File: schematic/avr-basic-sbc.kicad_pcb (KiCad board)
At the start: 2 copper layers, 94 x 55 mm, 38 parts, among them J1 DC-005 Power Jack, J2 PS/2 keyboard port, J3 RCA Video Jack, J4 Port B, J5 Port A, J6 Port C, J7 Port D, J8 USBasp header, J9 Power output header, U1 ATmega1284P-P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

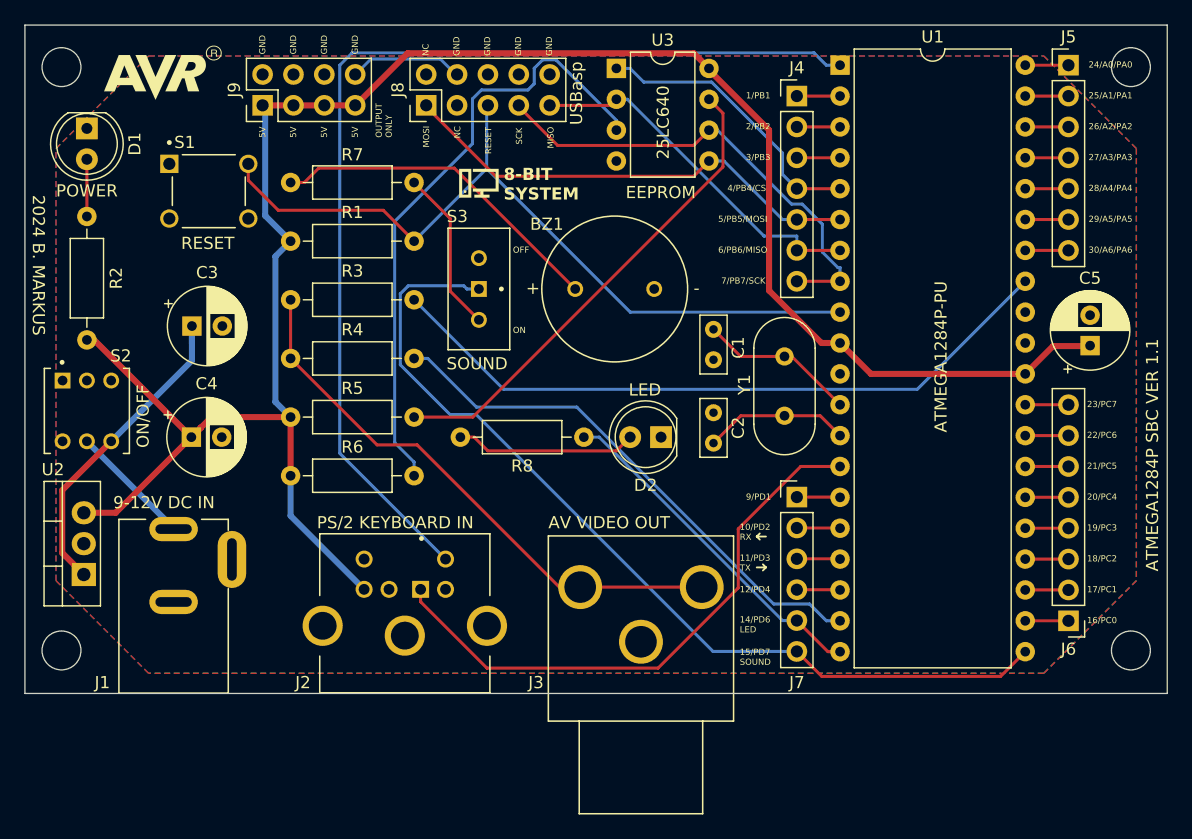
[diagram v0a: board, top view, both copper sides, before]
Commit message: AVR-SBC board updated - GPIO headers and IC-s realigned to match 0.254mm grid
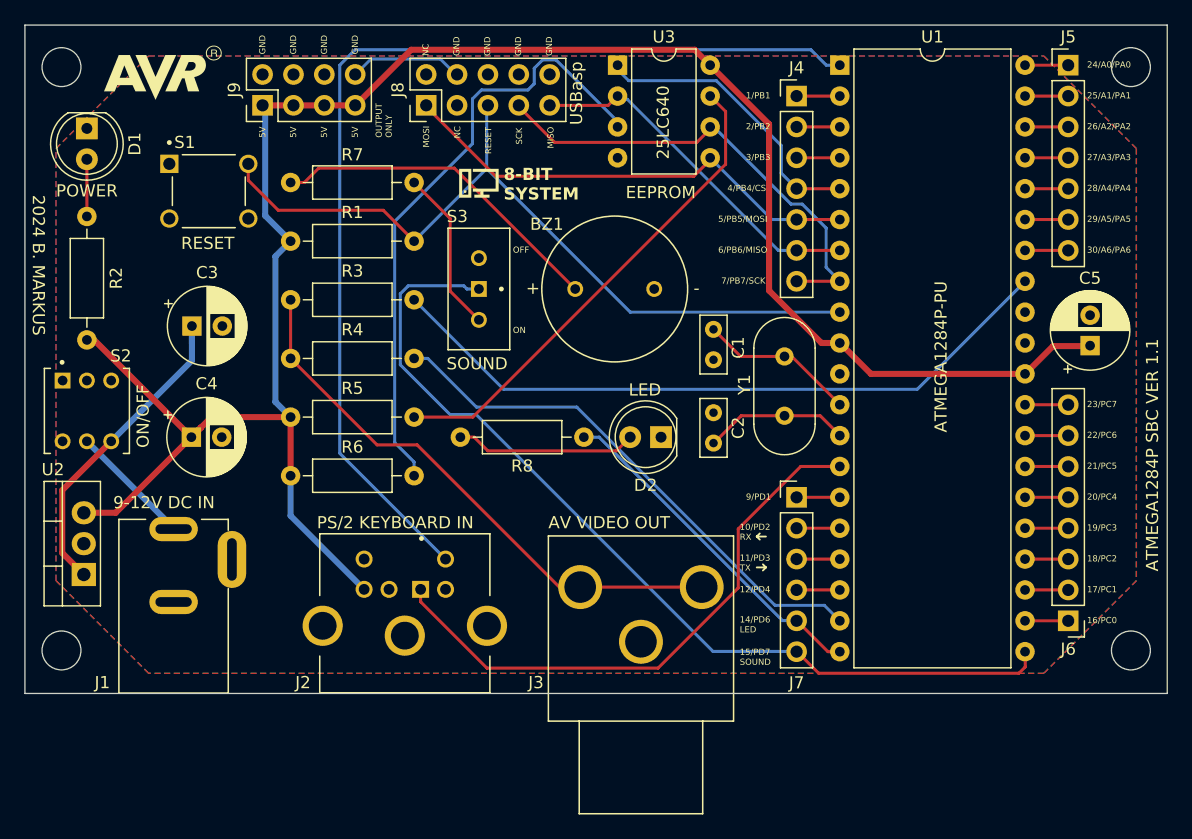
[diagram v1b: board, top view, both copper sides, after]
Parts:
- moved U3 0.28 mm to (48.8, 3.30)
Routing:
- net Net-(J7-Pin_6): track 75.6 -> 76.1 mm

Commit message: AVR-SBC board updated - Silkscreen updates and fill zones updated to match 1mm grid
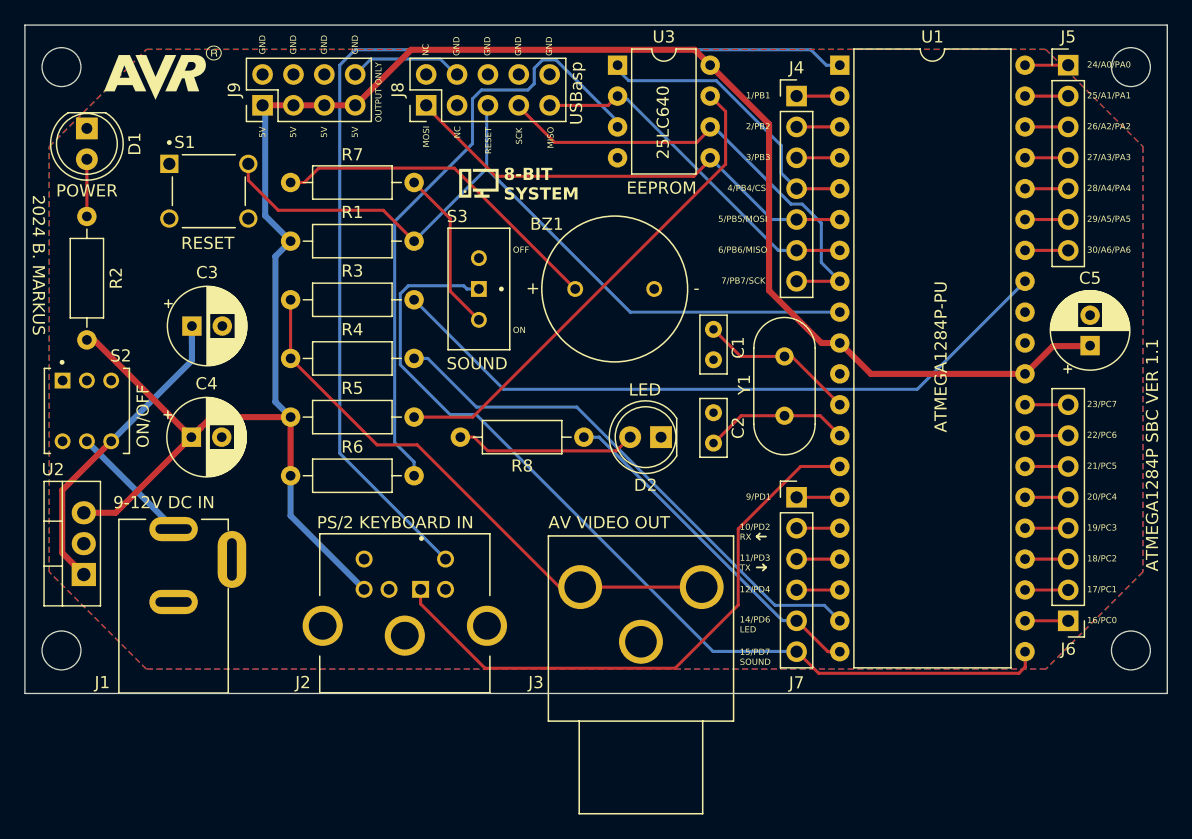
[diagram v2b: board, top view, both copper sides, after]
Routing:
- net Data: track 47.5 -> 48.4 mm
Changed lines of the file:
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@@
     (effects (font (size 0.508 0.508) (thickness 0.127)) (justify left bottom))
   )
-  (gr_text "OUTPUT\nONLY" (at 30.246 9.271 90) (layer "F.SilkS")
+  (gr_text "OUTPUT ONLY" (at 29.4 8 90) (layer "F.SilkS")
     (effects (font (size 0.508 0.508) (thickness 0.127)) (justify left bottom))
   )
@@
     (effects (font (size 0.508 0.508) (thickness 0.127)) (justify left bottom))
   )
-  (gr_text "EEPROM" (at 49.433 14.361) (layer "F.SilkS")
+  (gr_text "EEPROM" (at 49.5 14) (layer "F.SilkS")
     (effects (font (size 1 1) (thickness 0.15)) (justify left bottom))
   )
@@
   (segment (start 13.744 26.1854) (end 13.7442 26.1852) (width 0.5) (layer "B.Cu") (net 8))
   (segment (start 7.1 34.25) (end 13.744 27.6058) (width 0.5) (layer "B.Cu") (net 8))
-  (segment (start 58.6965 46.3158) (end 52.0945 52.9178) (width 0.25) (layer "F.Cu") (net 9))
-  (segment (start 38.0219 52.9178) (end 32.562 47.4579) (width 0.25) (layer "F.Cu") (net 9))
+  (segment (start 67.076 36.322) (end 63.8363 36.322) (width 0.25) (layer "F.Cu") (net 9))
+  (segment (start 58.6965 47.7295) (end 53.5082 52.9178) (width 0.25) (layer "F.Cu") (net 9))
+  (segment (start 53.5082 52.9178) (end 37.84985 52.9178) (width 0.25) (layer "F.Cu") (net 9))
+  (segment (start 37.84985 52.9178) (end 32.562 47.62995) (width 0.25) (layer "F.Cu") (net 9))
   (segment (start 63.8363 36.322) (end 58.6965 41.4618) (width 0.25) (layer "F.Cu") (net 9))
-  (segment (start 32.562 46.432) (end 32.562 47.4579) (width 0.25) (layer "F.Cu") (net 9))
-  (segment (start 52.0945 52.9178) (end 38.0219 52.9178) (width 0.25) (layer "F.Cu") (net 9))
-  (segment (start 67.076 36.322) (end 63.8363 36.322) (width 0.25) (layer "F.Cu") (net 9))
-  (segment (start 58.6965 41.4618) (end 58.6965 46.3158) (width 0.25) (layer "F.Cu") (net 9))
+  (segment (start 58.6965 41.4618) (end 58.6965 47.7295) (width 0.25) (layer "F.Cu") (net 9))
+  (segment (start 32.562 47.62995) (end 32.562 46.432) (width 0.25) (layer "F.Cu") (net 9))
   (segment (start 67.076 3.302) (end 65.9491 3.302) (width 0.25) (layer "B.Cu") (net 10))
   (segment (start 25.908 3.302) (end 25.908 35.238) (width 0.25) (layer "B.Cu") (net 10))
@@
   (segment (start 63.52 21.082) (end 67.076 21.082) (width 0.25) (layer "F.Cu") (net 17))
   (segment (start 63.03665 14.732) (end 63.9656 14.732) (width 0.25) (layer "B.Cu") (net 17))
+  (segment (start 63.9656 14.732) (end 65.532 16.2984) (width 0.25) (layer "B.Cu") (net 17))
+  (segment (start 56.95065 8.646) (end 63.03665 14.732) (width 0.25) (layer "B.Cu") (net 17))
+  (segment (start 65.532 19.538) (end 67.076 21.082) (width 0.25) (layer "B.Cu") (net 17))
   (segment (start 56.291 8.646) (end 56.95065 8.646) (width 0.25) (layer "B.Cu") (net 17))
-  (segment (start 63.9656 14.732) (end 65.931 16.6974) (width 0.25) (layer "B.Cu") (net 17))
-  (segment (start 65.931 19.937) (end 67.076 21.082) (width 0.25) (layer "B.Cu") (net 17))
-  (segment (start 56.95065 8.646) (end 63.03665 14.732) (width 0.25) (layer "B.Cu") (net 17))
-  (segment (start 65.931 16.6974) (end 65.931 19.937) (width 0.25) (layer "B.Cu") (net 17))
+  (segment (start 65.532 16.2984) (end 65.532 19.538) (width 0.25) (layer "B.Cu") (net 17))
   (segment (start 82.316 3.302) (end 85.872 3.302) (width 0.25) (layer "F.Cu") (net 18))
   (segment (start 82.316 5.842) (end 85.872 5.842) (width 0.25) (layer "F.Cu") (net 19))
@@
     (polygon
       (pts
-        (xy 2.56 10.16)
-        (xy 10.18 2.54)
-        (xy 83.84 2.54)
-        (xy 91.46 10.16)
-        (xy 91.46 45.72)
-        (xy 83.84 53.34)
-        (xy 10.18 53.34)
-        (xy 2.56 45.72)
+        (xy 2 10)
+        (xy 10 2)
+        (xy 84 2)
+        (xy 92 10)
+        (xy 92 45)
+        (xy 84 53)
+        (xy 10 53)
+        (xy 2 45)
       )
     )

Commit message: AVR-SBC board updated - Mounting holes aligned to match 1mm grid
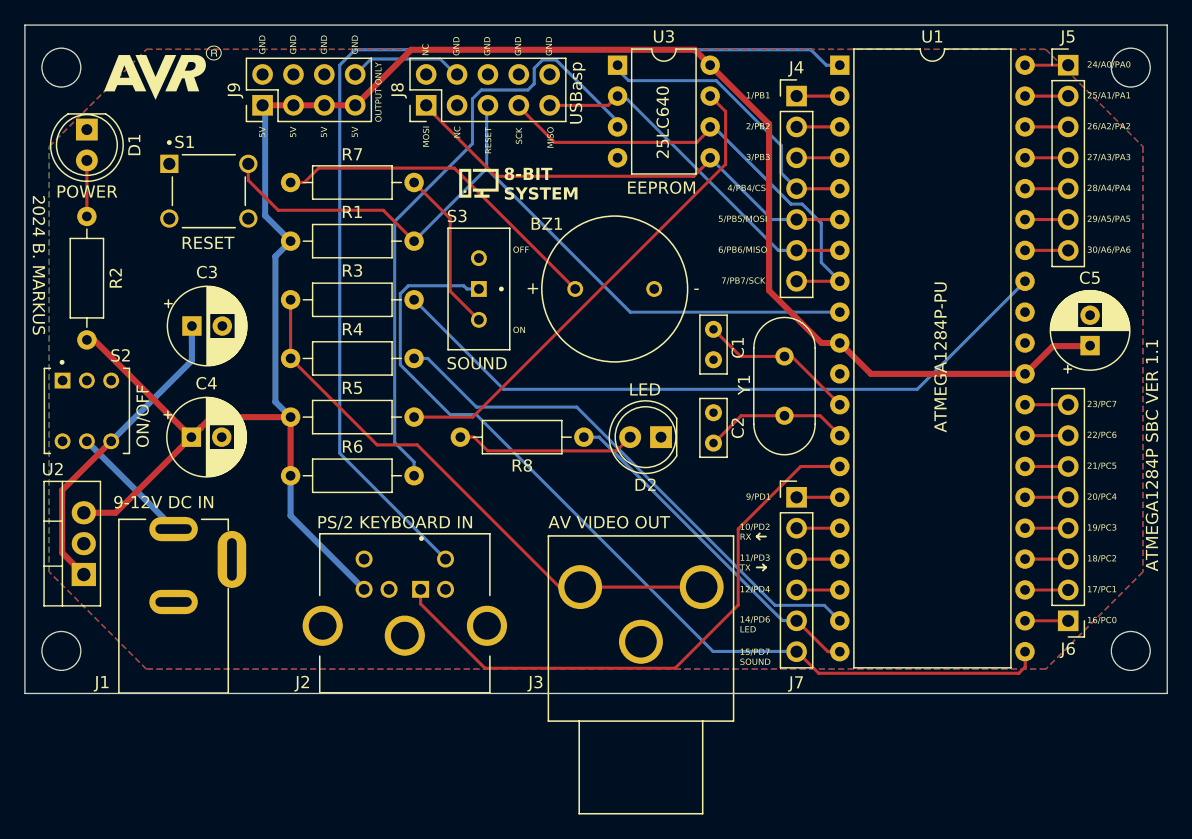
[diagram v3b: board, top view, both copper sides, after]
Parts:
- moved D1 0.10 mm to (5.10, 8.60)
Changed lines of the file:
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@@
   (net 58 "Net-(J3-Video)")
   (footprint "MountingHole:MountingHole_3.2mm_M3_DIN965" (layer "F.Cu")
-    (at 3.01 51.46)
+    (at 3 51.5)
     (descr "Mounting Hole 3.2mm, no annular, M3, DIN965")
     (tags "mounting hole 3.2mm no annular m3 din965")
@@
   )
   (footprint "MountingHole:MountingHole_3.2mm_M3_DIN965" (layer "F.Cu")
-    (at 91.01 3.46)
+    (at 91 3.5)
     (descr "Mounting Hole 3.2mm, no annular, M3, DIN965")
     (tags "mounting hole 3.2mm no annular m3 din965")
@@
   )
   (footprint "MountingHole:MountingHole_3.2mm_M3_DIN965" (layer "F.Cu")
-    (at 3.01 3.46)
+    (at 3 3.5)
     (descr "Mounting Hole 3.2mm, no annular, M3, DIN965")
     (tags "mounting hole 3.2mm no annular m3 din965")
@@
   )
   (footprint "StockLib:LED_D5.0mm_RED" (layer "F.Cu")
-    (at 5.1 8.504 -90)
+    (at 5.1 8.6 -90)
     (descr "LED, diameter 5.0mm, 2 pins, http://cdn-reichelt.de/documents/datenblatt/A500/LL-504BC2E-009.pdf")
     (tags "LED diameter 5.0mm 2 pins")
@@
   )
   (footprint "MountingHole:MountingHole_3.2mm_M3_DIN965" (layer "F.Cu")
-    (at 91.01 51.46)
+    (at 91 51.5)
     (descr "Mounting Hole 3.2mm, no annular, M3, DIN965")
     (tags "mounting hole 3.2mm no annular m3 din965")
@@
     (effects (font (size 0.508 0.508) (thickness 0.127)) (justify left bottom))
   )
-  (gr_text "POWER" (at 2.56 14.224) (layer "F.SilkS")
+  (gr_text "POWER" (at 2.56 14.32) (layer "F.SilkS")
     (effects (font (size 1 1) (thickness 0.15)) (justify left bottom))
   )

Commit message: AVR-SBC board updated: Connectors moved closer to each other to leave space for shields
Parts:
- moved J3 3.70 mm to (47.0, 52.0)
- moved J2 2.26 mm to (29.0, 50.2)
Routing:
- net Video: track 57.0 -> 63.8 mm
- net Net-(J3-Video): track 46.4 -> 43.3 mm
- net Data: track 48.4 -> 50.5 mm
- net +5V: track 167.4 -> 166.4 mm
- net Clock: track 86.5 -> 85.5 mm
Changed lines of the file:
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@@
   )
   (footprint "StockLib:PS2-connector-keyboard" (layer "F.Cu")
-    (at 31.262 50.242)
+    (at 29 50.242)
     (property "Availability" "In Stock")
     (property "Check_prices" "https://www.snapeda.com/parts/5749180-1/TE+Connectivity+AMP+Connectors/view-part/?ref=eda")
@@
   )
   (footprint "StockLib:RCA Video Jack" (layer "F.Cu")
-    (at 50.693 52.197 90)
+    (at 47 52.05 90)
     (descr "<b>DC POWER JACK</b><p>Source: DCJ0202.pdf")
     (property "MANUFACTURER" "CUI Inc")
@@
     (effects (font (size 0.508 0.508) (thickness 0.127)) (justify left bottom))
   )
-  (gr_text "PS/2 KEYBOARD IN" (at 24.023 41.529) (layer "F.SilkS")
+  (gr_text "PS/2 KEYBOARD IN" (at 21.6 41.529) (layer "F.SilkS")
     (effects (font (size 1 1) (thickness 0.15)) (justify left bottom))
   )
@@
     (effects (font (size 0.508 0.508) (thickness 0.127)) (justify left bottom))
   )
-  (gr_text "AV VIDEO OUT" (at 43.073 41.529) (layer "F.SilkS")
+  (gr_text "AV VIDEO OUT" (at 39.8 41.529) (layer "F.SilkS")
     (effects (font (size 1 1) (thickness 0.15)) (justify left bottom))
   )
@@
   (segment (start 7.4736 40.132) (end 13.697 33.909) (width 0.5) (layer "F.Cu") (net 6))
   (segment (start 15.348 32.258) (end 14.4968 33.1092) (width 0.5) (layer "F.Cu") (net 6))
-  (segment (start 21.864 40.384) (end 27.912 46.432) (width 0.5) (layer "B.Cu") (net 6))
+  (segment (start 25.65 46.328) (end 25.65 46.432) (width 0.5) (layer "B.Cu") (net 6))
+  (segment (start 21.864 37.084) (end 21.864 42.542) (width 0.5) (layer "B.Cu") (net 6))
   (segment (start 19.7665 6.8125) (end 19.7665 15.6825) (width 0.5) (layer "B.Cu") (net 6))
-  (segment (start 21.864 37.084) (end 21.864 40.384) (width 0.5) (layer "B.Cu") (net 6))
+  (segment (start 21.864 42.542) (end 25.65 46.328) (width 0.5) (layer "B.Cu") (net 6))
   (segment (start 19.588 6.604) (end 19.558 6.604) (width 0.5) (layer "B.Cu") (net 6))
   (segment (start 20.6121 19.0319) (end 21.864 17.78) (width 0.5) (layer "B.Cu") (net 6))
@@
   (segment (start 13.744 26.1854) (end 13.7442 26.1852) (width 0.5) (layer "B.Cu") (net 8))
   (segment (start 7.1 34.25) (end 13.744 27.6058) (width 0.5) (layer "B.Cu") (net 8))
-  (segment (start 67.076 36.322) (end 63.8363 36.322) (width 0.25) (layer "F.Cu") (net 9))
+  (segment (start 35.8998 52.9178) (end 30.3 47.318) (width 0.25) (layer "F.Cu") (net 9))
   (segment (start 58.6965 47.7295) (end 53.5082 52.9178) (width 0.25) (layer "F.Cu") (net 9))
-  (segment (start 53.5082 52.9178) (end 37.84985 52.9178) (width 0.25) (layer "F.Cu") (net 9))
-  (segment (start 37.84985 52.9178) (end 32.562 47.62995) (width 0.25) (layer "F.Cu") (net 9))
+  (segment (start 30.3 47.318) (end 30.3 46.432) (width 0.25) (layer "F.Cu") (net 9))
+  (segment (start 67.076 36.322) (end 63.8363 36.322) (width 0.25) (layer "F.Cu") (net 9))
   (segment (start 63.8363 36.322) (end 58.6965 41.4618) (width 0.25) (layer "F.Cu") (net 9))
   (segment (start 58.6965 41.4618) (end 58.6965 47.7295) (width 0.25) (layer "F.Cu") (net 9))
-  (segment (start 32.562 47.62995) (end 32.562 46.432) (width 0.25) (layer "F.Cu") (net 9))
-  (segment (start 67.076 3.302) (end 65.9491 3.302) (width 0.25) (layer "B.Cu") (net 10))
-  (segment (start 25.908 3.302) (end 25.908 35.238) (width 0.25) (layer "B.Cu") (net 10))
+  (segment (start 53.5082 52.9178) (end 35.8998 52.9178) (width 0.25) (layer "F.Cu") (net 9))
   (segment (start 64.6791 2.032) (end 27.178 2.032) (width 0.25) (layer "B.Cu") (net 10))
-  (segment (start 25.908 35.238) (end 34.612 43.942) (width 0.25) (layer "B.Cu") (net 10))
+  (segment (start 25.908 37.5) (end 32.35 43.942) (width 0.25) (layer "B.Cu") (net 10))
   (segment (start 27.178 2.032) (end 25.908 3.302) (width 0.25) (layer "B.Cu") (net 10))
+  (segment (start 25.908 3.302) (end 25.908 37.5) (width 0.25) (layer "B.Cu") (net 10))
+  (segment (start 67.076 3.302) (end 65.9491 3.302) (width 0.25) (layer "B.Cu") (net 10))
   (segment (start 65.9491 3.302) (end 64.6791 2.032) (width 0.25) (layer "B.Cu") (net 10))
   (segment (start 63.52 5.842) (end 67.076 5.842) (width 0.25) (layer "F.Cu") (net 11))
@@
   (segment (start 82.316 51.562) (end 82.316 52.812) (width 0.25) (layer "F.Cu") (net 38))
   (segment (start 81.788 53.34) (end 65.318 53.34) (width 0.25) (layer "F.Cu") (net 38))
+  (segment (start 30.8897 22.1121) (end 31.5451 21.4567) (width 0.25) (layer "B.Cu") (net 38))
+  (segment (start 39.878 32.512) (end 35.4443 32.512) (width 0.25) (layer "B.Cu") (net 38))
+  (segment (start 36.3771 21.717) (end 37.358 21.717) (width 0.25) (layer "B.Cu") (net 38))
+  (segment (start 63.4796 51.5416) (end 48.006 36.068) (width 0.25) (layer "B.Cu") (net 38))
+  (segment (start 35.4443 32.512) (end 30.8897 27.9574) (width 0.25) (layer "B.Cu") (net 38))
   (segment (start 30.8897 27.9574) (end 30.8897 22.1121) (width 0.25) (layer "B.Cu") (net 38))
-  (segment (start 37.358 21.717) (end 36.3771 21.717) (width 0.25) (layer "B.Cu") (net 38))
-  (segment (start 63.52 51.5416) (end 56.6236 51.5416) (width 0.25) (layer "B.Cu") (net 38))
   (segment (start 31.5451 21.4567) (end 36.1168 21.4567) (width 0.25) (layer "B.Cu") (net 38))
-  (segment (start 37.1301 32.0481) (end 34.9804 32.0481) (width 0.25) (layer "B.Cu") (net 38))
-  (segment (start 34.9804 32.0481) (end 30.8897 27.9574) (width 0.25) (layer "B.Cu") (net 38))
-  (segment (start 56.6236 51.5416) (end 37.1301 32.0481) (width 0.25) (layer "B.Cu") (net 38))
-  (segment (start 30.8897 22.1121) (end 31.5451 21.4567) (width 0.25) (layer "B.Cu") (net 38))
+  (segment (start 43.434 36.068) (end 39.878 32.512) (width 0.25) (layer "B.Cu") (net 38))
+  (segment (start 63.52 51.5416) (end 63.4796 51.5416) (width 0.25) (layer "B.Cu") (net 38))
   (segment (start 36.1168 21.4567) (end 36.3771 21.717) (width 0.25) (layer "B.Cu") (net 38))
+  (segment (start 48.006 36.068) (end 43.434 36.068) (width 0.25) (layer "B.Cu") (net 38))
   (segment (start 29.484 15.24) (end 32.024 17.78) (width 0.25) (layer "F.Cu") (net 41))
   (segment (start 18.383 12.775) (end 20.848 15.24) (width 0.25) (layer "F.Cu") (net 41))
@@
   (segment (start 32.024 17.78) (end 37.998 11.806) (width 0.25) (layer "B.Cu") (net 41))
   (segment (start 37.998 11.806) (end 37.998 6.609) (width 0.25) (layer "B.Cu") (net 41))
-  (segment (start 73.426 29.972) (end 39.39 29.972) (width 0.25) (layer "B.Cu") (net 42))
-  (segment (start 39.39 29.972) (end 32.024 22.606) (width 0.25) (layer "B.Cu") (net 42))
-  (segment (start 82.316 21.082) (end 73.426 29.972) (width 0.25) (layer "B.Cu") (net 42))
+  (segment (start 39.39 29.972) (end 82.804 29.972) (width 0.25) (layer "B.Cu") (net 42))
+  (segment (start 82.804 29.972) (end 83.82 28.956) (width 0.25) (layer "B.Cu") (net 42))
+  (segment (start 83.82 28.956) (end 83.82 22.606) (width 0.25) (layer "B.Cu") (net 42))
+  (segment (start 32.024 22.606) (end 39.39 29.972) (width 0.25) (layer "B.Cu") (net 42))
+  (segment (start 83.82 22.606) (end 82.296 21.082) (width 0.25) (layer "B.Cu") (net 42))
   (segment (start 65.786 47.752) (end 61.7305 47.752) (width 0.25) (layer "B.Cu") (net 43))
   (segment (start 61.7305 47.752) (end 45.4154 31.4369) (width 0.25) (layer "B.Cu") (net 43))
@@
   (segment (start 49.804 33.909) (end 48.6757 35.0373) (width 0.25) (layer "F.Cu") (net 55))
   (segment (start 48.6757 35.0373) (end 38.0892 35.0373) (width 0.25) (layer "F.Cu") (net 55))
-  (segment (start 43.981 46.247) (end 45.693 46.247) (width 0.25) (layer "F.Cu") (net 58))
+  (segment (start 43.981 46.247) (end 52.5 46.247) (width 0.25) (layer "F.Cu") (net 58))
+  (segment (start 32.278 34.544) (end 43.981 46.247) (width 0.25) (layer "F.Cu") (net 58))
   (segment (start 28.976 34.544) (end 32.278 34.544) (width 0.25) (layer "F.Cu") (net 58))
   (segment (start 21.864 27.432) (end 28.976 34.544) (width 0.25) (layer "F.Cu") (net 58))
-  (segment (start 32.278 34.544) (end 43.981 46.247) (width 0.25) (layer "F.Cu") (net 58))
   (segment (start 21.864 22.606) (end 21.864 27.432) (width 0.25) (layer "F.Cu") (net 58))
-  (segment (start 45.693 46.247) (end 55.693 46.247) (width 0.25) (layer "F.Cu") (net 58))
   (zone (net 2) (net_name "GND") (layers "F&B.Cu") (hatch edge 0.5)
     (connect_pads (clearance 0.5))
